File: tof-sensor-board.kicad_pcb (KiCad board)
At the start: 2 copper layers, 20 x 12 mm, 27 parts, among them U1 STM32F302K8U6, U2 LTC2875, U4 VL53L0X, X1 16MHz

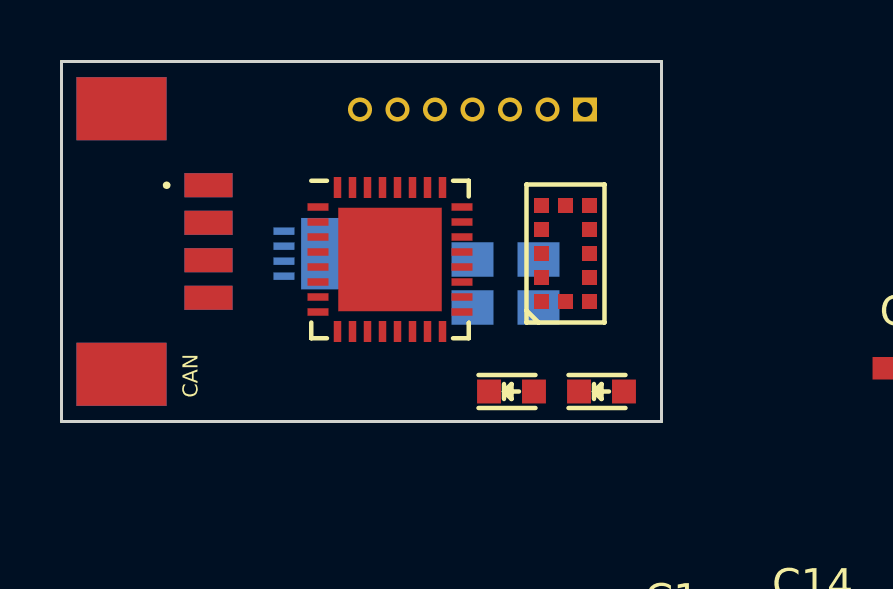
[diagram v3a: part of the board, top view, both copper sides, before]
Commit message: LDO footprint, fix unconnected GND pin
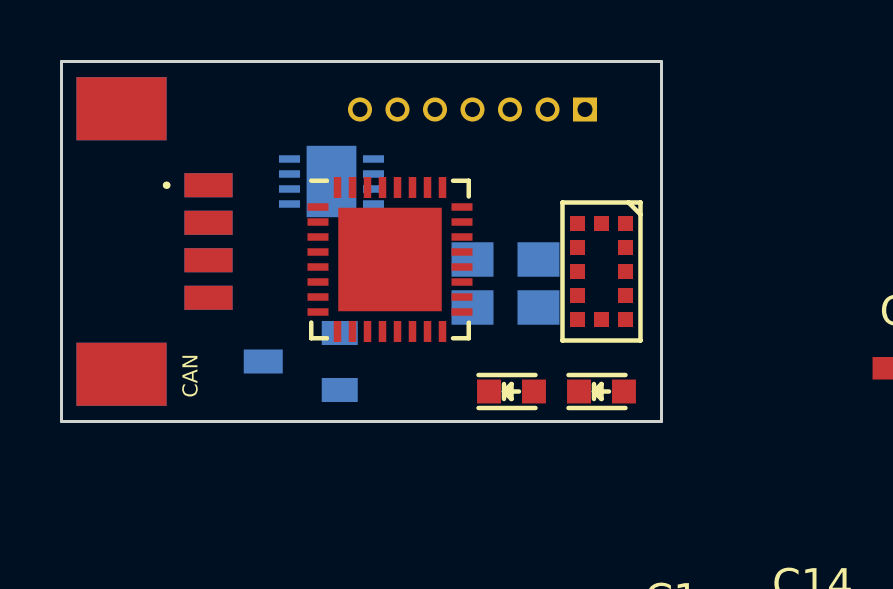
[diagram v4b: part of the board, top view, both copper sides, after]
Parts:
- added U3: MCP1703, _std:SOT-23, B.Cu at (39.0, 33.0)
- moved U2 2.41 mm to (40.0, 27.0)
- moved U4 1.34 mm to (49.0, 30.0), turned to 90 degrees
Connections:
- U4 pad 6: (no net) -> GND
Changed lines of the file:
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@@
 (kicad_pcb (version 4) (host pcbnew 4.0.1-stable)
   (general
-    (links 82)
-    (no_connects 82)
+    (links 86)
+    (no_connects 86)
     (area 30.949999 22.949999 51.050001 35.050001)
     (thickness 1.6)
@@
     (tracks 0)
     (zones 0)
-    (modules 27)
+    (modules 28)
     (nets 26)
   )
@@
   )
   (module Housings_DFN_QFN:DFN-8-1EP_3x3mm_Pitch0.5mm (layer B.Cu)
-    (at 39.815 29.405 180)
+    (at 40 27 180)
     (descr "DD Package; 8-Lead Plastic DFN (3mm x 3mm) (see Linear Technology DFN_8_05-08-1698.pdf)")
     (tags "DFN 0.5")
@@
   )
   (module _sensors:VL53L0X (layer F.Cu)
-    (at 47.8 29.4 270)
+    (at 49 30 90)
     (descr VL53L0X)
     (tags "TOF distance sensor")
-    (fp_text reference U4 (at 0 0 270) (layer F.SilkS) hide
+    (fp_text reference U4 (at 0 0 90) (layer F.SilkS) hide
       (effects (font (size 0.5 0.5) (thickness 0.125)))
     )
-    (fp_text value VL53L0X (at 0 0 270) (layer F.Fab) hide
+    (fp_text value VL53L0X (at 0 0 90) (layer F.Fab) hide
       (effects (font (size 0.5 0.5) (thickness 0.125)))
     )
@@
     (fp_line (start -2.3 -1.3) (end -2.3 1.3) (layer F.SilkS) (width 0.15))
     (fp_line (start 2.3 -1.3) (end -2.3 -1.3) (layer F.SilkS) (width 0.15))
-    (pad 1 smd rect (at 1.6 0.8 270) (size 0.5 0.5) (layers F.Cu F.Paste F.Mask)
-      (net 1 VCC))
-    (pad 2 smd rect (at 0.8 0.8 270) (size 0.5 0.5) (layers F.Cu F.Paste F.Mask)
-      (net 2 GND))
-    (pad 3 smd rect (at 0 0.8 270) (size 0.5 0.5) (layers F.Cu F.Paste F.Mask)
-      (net 2 GND))
-    (pad 5 smd rect (at -1.6 0.8 270) (size 0.5 0.5) (layers F.Cu F.Paste F.Mask)
+    (pad 1 smd rect (at 1.6 0.8 90) (size 0.5 0.5) (layers F.Cu F.Paste F.Mask)
+      (net 1 VCC))
+    (pad 2 smd rect (at 0.8 0.8 90) (size 0.5 0.5) (layers F.Cu F.Paste F.Mask)
+      (net 2 GND))
+    (pad 3 smd rect (at 0 0.8 90) (size 0.5 0.5) (layers F.Cu F.Paste F.Mask)
+      (net 2 GND))
+    (pad 5 smd rect (at -1.6 0.8 90) (size 0.5 0.5) (layers F.Cu F.Paste F.Mask)
       (net 22 /XSHUT))
-    (pad 4 smd rect (at -0.8 0.8 270) (size 0.5 0.5) (layers F.Cu F.Paste F.Mask)
-      (net 2 GND))
-    (pad 6 smd rect (at -1.6 0 270) (size 0.5 0.5) (layers F.Cu F.Paste F.Mask))
-    (pad 11 smd rect (at 1.6 -0.8 270) (size 0.5 0.5) (layers F.Cu F.Paste F.Mask)
-      (net 1 VCC))
-    (pad 10 smd rect (at 0.8 -0.8 270) (size 0.5 0.5) (layers F.Cu F.Paste F.Mask)
+    (pad 4 smd rect (at -0.8 0.8 90) (size 0.5 0.5) (layers F.Cu F.Paste F.Mask)
+      (net 2 GND))
+    (pad 6 smd rect (at -1.6 0 90) (size 0.5 0.5) (layers F.Cu F.Paste F.Mask)
+      (net 2 GND))
+    (pad 11 smd rect (at 1.6 -0.8 90) (size 0.5 0.5) (layers F.Cu F.Paste F.Mask)
+      (net 1 VCC))
+    (pad 10 smd rect (at 0.8 -0.8 90) (size 0.5 0.5) (layers F.Cu F.Paste F.Mask)
       (net 16 /I2C_SCL))
-    (pad 9 smd rect (at 0 -0.8 270) (size 0.5 0.5) (layers F.Cu F.Paste F.Mask)
+    (pad 9 smd rect (at 0 -0.8 90) (size 0.5 0.5) (layers F.Cu F.Paste F.Mask)
       (net 17 /I2C_SDA))
-    (pad 8 smd rect (at -0.8 -0.8 270) (size 0.5 0.5) (layers F.Cu F.Paste F.Mask))
-    (pad 7 smd rect (at -1.6 -0.8 270) (size 0.5 0.5) (layers F.Cu F.Paste F.Mask)
+    (pad 8 smd rect (at -0.8 -0.8 90) (size 0.5 0.5) (layers F.Cu F.Paste F.Mask))
+    (pad 7 smd rect (at -1.6 -0.8 90) (size 0.5 0.5) (layers F.Cu F.Paste F.Mask)
       (net 15 /GPIO1))
-    (pad 12 smd rect (at 1.6 0 270) (size 0.5 0.5) (layers F.Cu F.Paste F.Mask)
+    (pad 12 smd rect (at 1.6 0 90) (size 0.5 0.5) (layers F.Cu F.Paste F.Mask)
       (net 2 GND))
   )
@@
     )
   )
+  (module _std:SOT-23 (layer B.Cu)
+    (at 39 33 270)
+    (descr "SOT-23, Standard")
+    (tags SOT-23)
+    (attr smd)
+    (fp_text reference U3 (at 0 3 270) (layer B.SilkS) hide
+      (effects (font (size 1 1) (thickness 0.15)) (justify mirror))
+    )
+    (fp_text value MCP1703 (at 0 -3 270) (layer B.Fab) hide
+      (effects (font (size 1 1) (thickness 0.15)) (justify mirror))
+    )
+    (fp_line (start 1.29916 0.65024) (end 1.2509 0.65024) (layer B.SilkS) (width 0.15))
+    (fp_line (start -1.49982 -0.0508) (end -1.49982 0.65024) (layer B.SilkS) (width 0.15))
+    (fp_line (start -1.49982 0.65024) (end -1.2509 0.65024) (layer B.SilkS) (width 0.15))
+    (fp_line (start 1.29916 0.65024) (end 1.49982 0.65024) (layer B.SilkS) (width 0.15))
+    (fp_line (start 1.49982 0.65024) (end 1.49982 -0.0508) (layer B.SilkS) (width 0.15))
+    (pad 1 smd rect (at -0.95 -1.275 270) (size 0.8 1.2) (layers B.Cu B.Paste B.Mask)
+      (net 2 GND))
+    (pad 2 smd rect (at 0.95 -1.275 270) (size 0.8 1.2) (layers B.Cu B.Paste B.Mask)
+      (net 1 VCC))
+    (pad 3 smd rect (at 0 1.275 270) (size 0.8 1.3) (layers B.Cu B.Paste B.Mask)
+      (net 4 +5V))
+    (model Housings_SOT-23_SOT-143_TSOT-6.3dshapes/SOT-23.wrl
+      (at (xyz 0 0 0))
+      (scale (xyz 1 1 1))
+      (rotate (xyz 0 0 0))
+    )
+  )

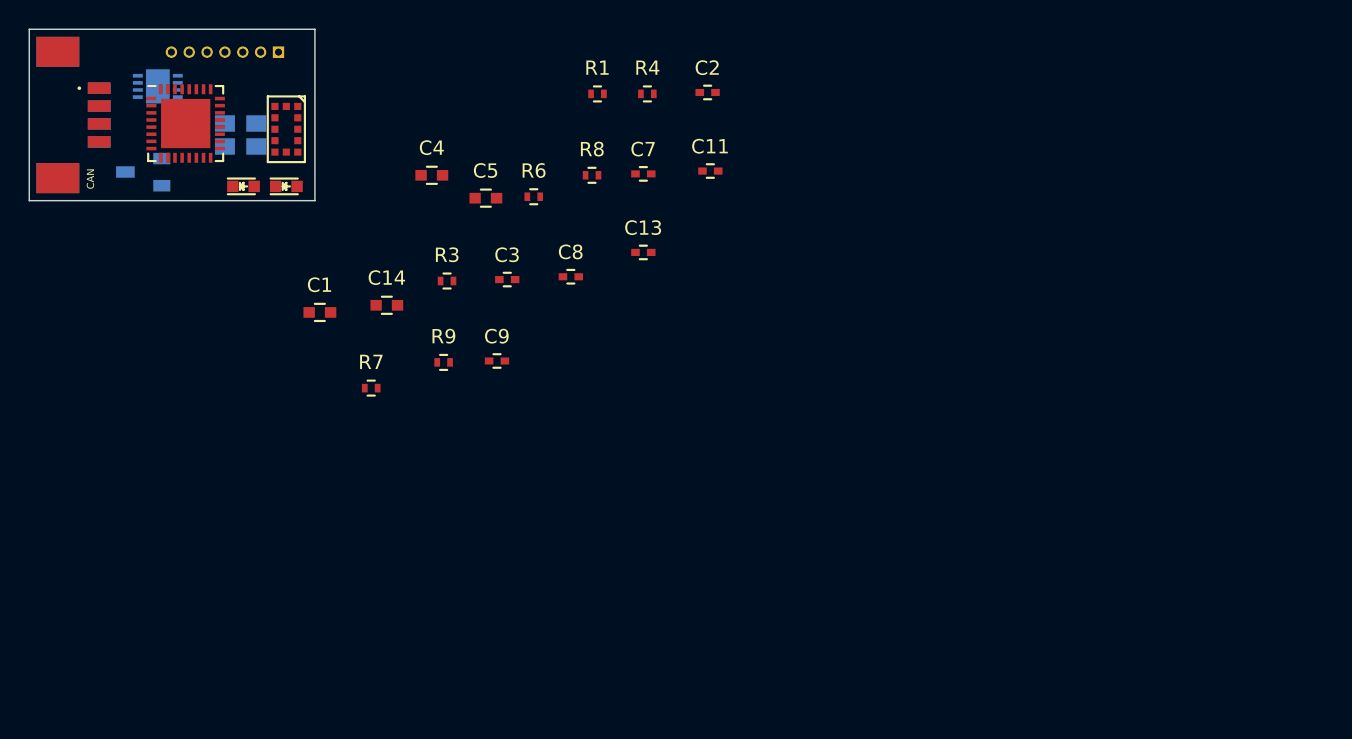
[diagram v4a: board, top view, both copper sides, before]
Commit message: Place mounting holes
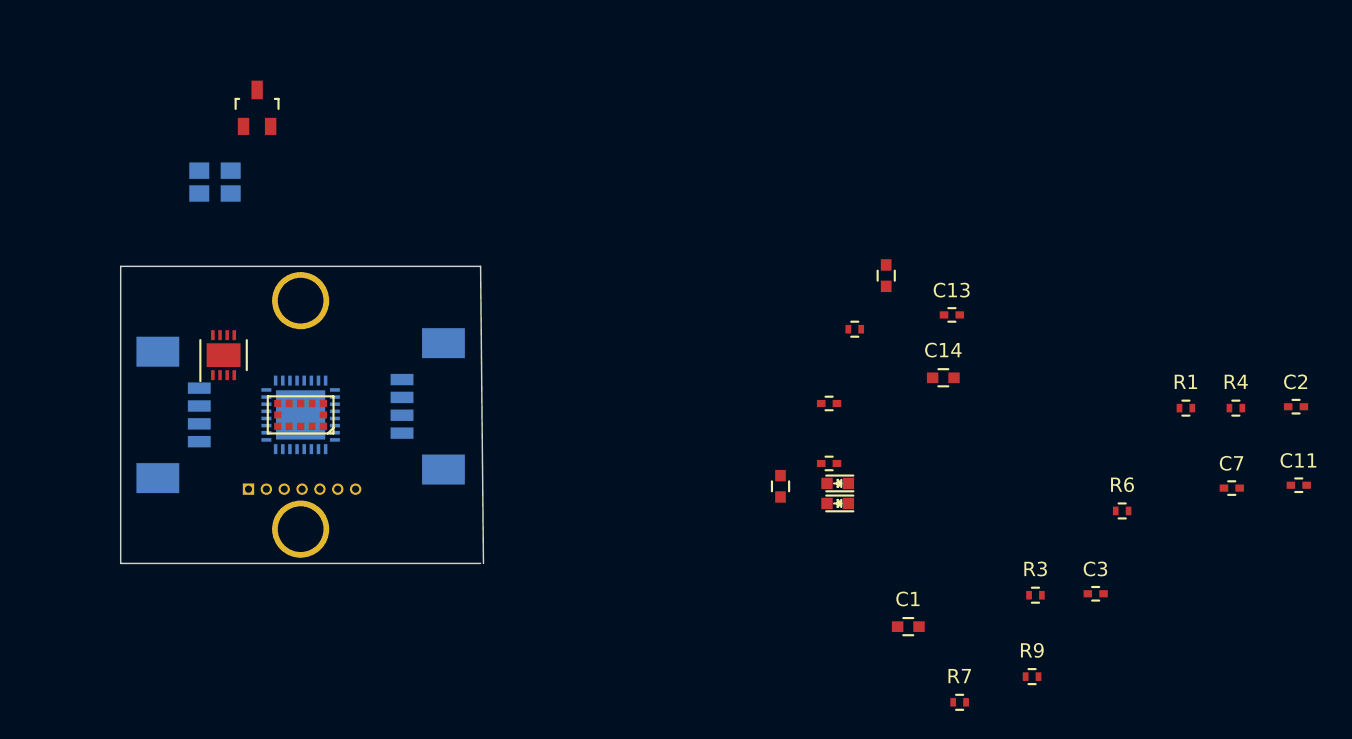
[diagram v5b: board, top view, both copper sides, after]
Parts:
- added CVRA-HOLE: VAL**, cvra:CVRA-HOLE, F.Cu at (50.0, 42.0)
- added CVRA-HOLE: VAL**, cvra:CVRA-HOLE, F.Cu at (50.0, 58.0)
- CONN3, U1: moved to B.Cu
- U2, U3: moved to F.Cu
- moved D2 47.2 mm to (87.6, 56.2), turned to 180 degrees
- moved R3 46.7 mm to (101.5, 62.6)
- moved R7 46.7 mm to (96.1, 70.1)
- moved R9 46.7 mm to (101.2, 68.3)
- moved C1 46.7 mm to (92.5, 64.8)
- moved C2 46.7 mm to (119.7, 49.4)
- moved C3 46.7 mm to (105.7, 62.5)
- moved C7 46.7 mm to (115.2, 55.1)
- moved R4 46.7 mm to (115.5, 49.5)
- moved R6 46.7 mm to (107.5, 56.7)
- moved C11 46.7 mm to (119.9, 54.9)
- moved R1 46.7 mm to (112.0, 49.5)
- moved D3 43.8 mm to (87.6, 54.8), turned to 180 degrees
- moved C14 39.3 mm to (95.0, 47.4)
- moved CONN3 33.8 mm to (60.0, 49.4)
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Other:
- board size 20 x 12 mm -> 25.4 x 20.8 mm
- net class Default: clearance 0.2 -> 0.16; trace_width 0.25 -> 0.16; via_drill 0.4 -> 0.3
- rule trace_clearance: 0.2 -> 0.16
- rule trace_min: 0.15 -> 0.1524
- rule via_min_size: 0.4 -> 0.6

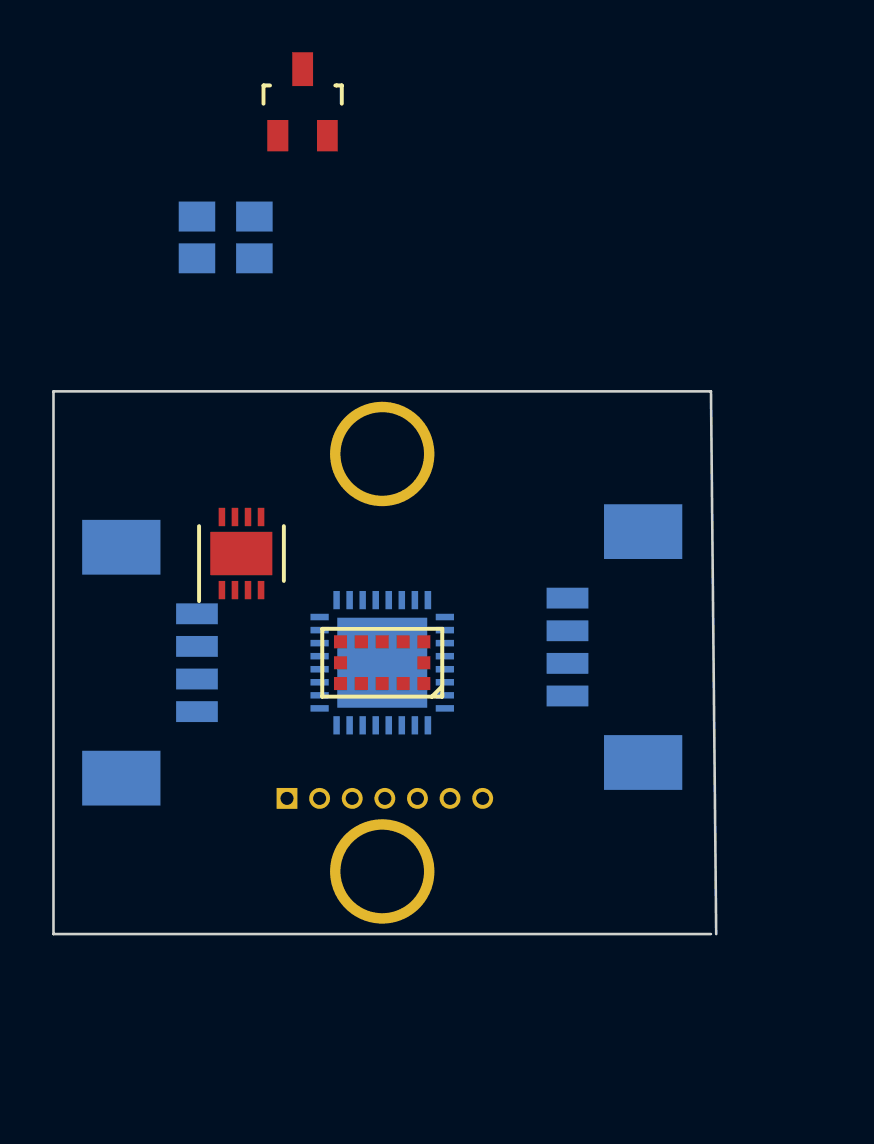
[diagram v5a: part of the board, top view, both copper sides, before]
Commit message: elongated shape with connectors on same edge
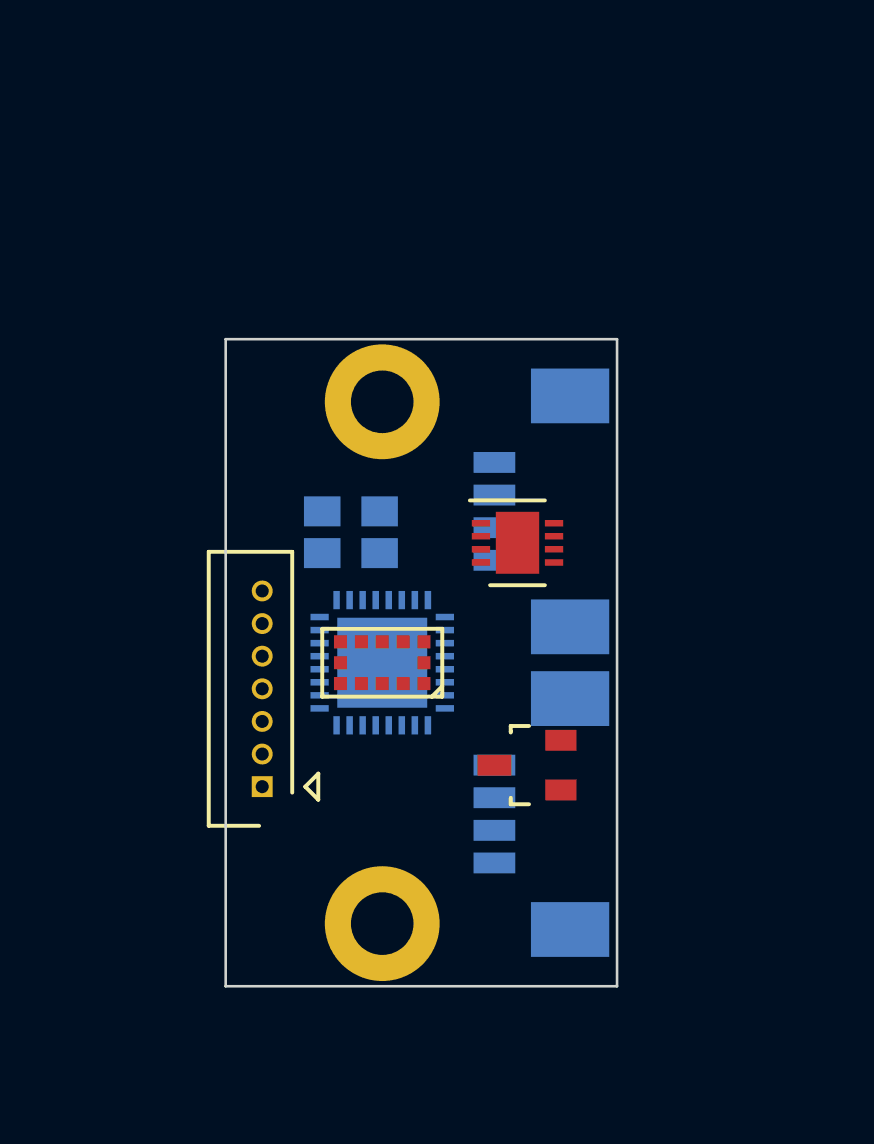
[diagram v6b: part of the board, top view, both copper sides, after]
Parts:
- removed CVRA-HOLE (x2): VAL**, cvra:CVRA-HOLE
- added _M2: VAL**, _mech:_M2, F.Cu at (50.4, 40.0)
- added _M2: VAL**, _mech:_M2, F.Cu at (50.0, 60.0)
- CONN1: moved to F.Cu
- moved U3 26.8 mm to (55.6, 53.9), turned to 90 degrees
- moved CONN2 18.2 mm to (57.2, 44.2), turned to 270 degrees
- moved X1 12.3 mm to (48.8, 45.0)
- moved U2 10.6 mm to (55.2, 45.4), turned to 0 degrees
- moved CONN3 6.99 mm to (57.2, 55.8)
- moved CONN1 1.05 mm to (45.4, 54.8), turned to 90 degrees
- turned U1 to 270 degrees
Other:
- board size 25.4 x 20.8 mm -> 15 x 24.8 mm

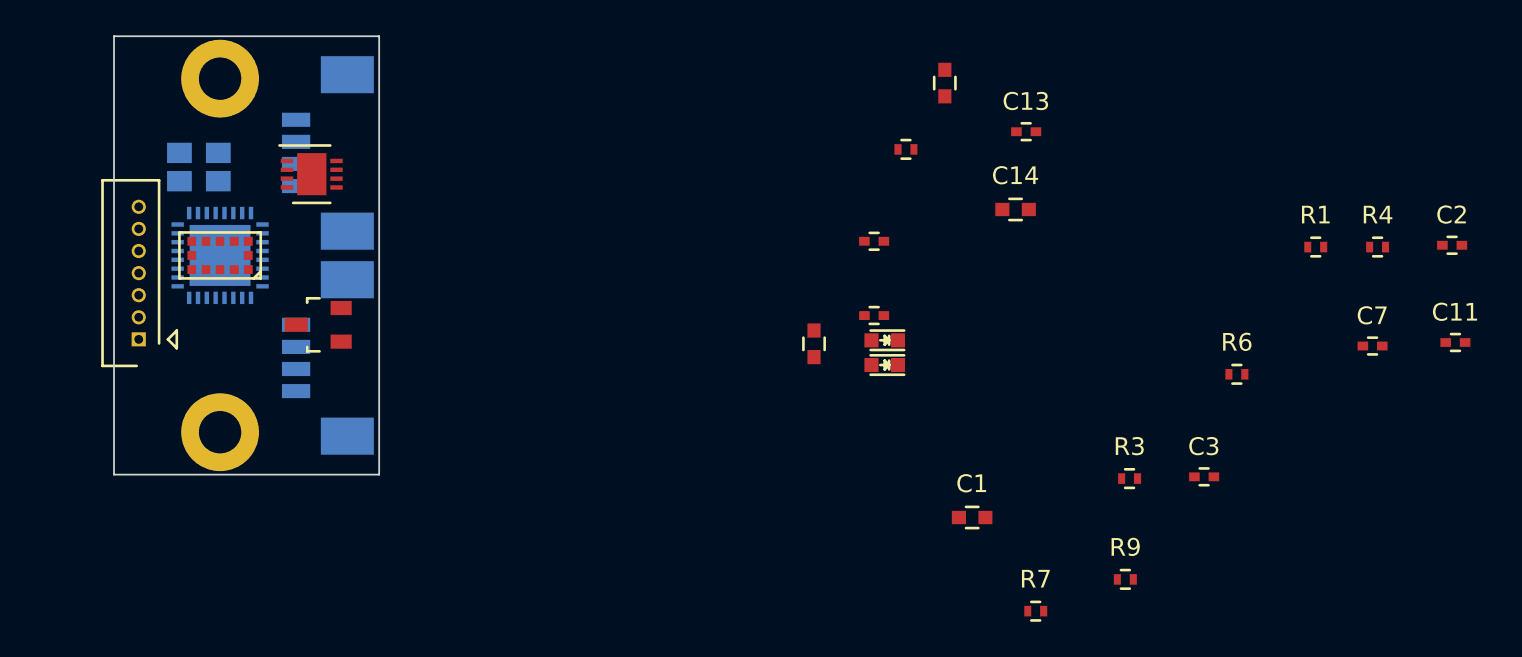
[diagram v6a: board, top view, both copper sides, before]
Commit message: mounting holes on same edge
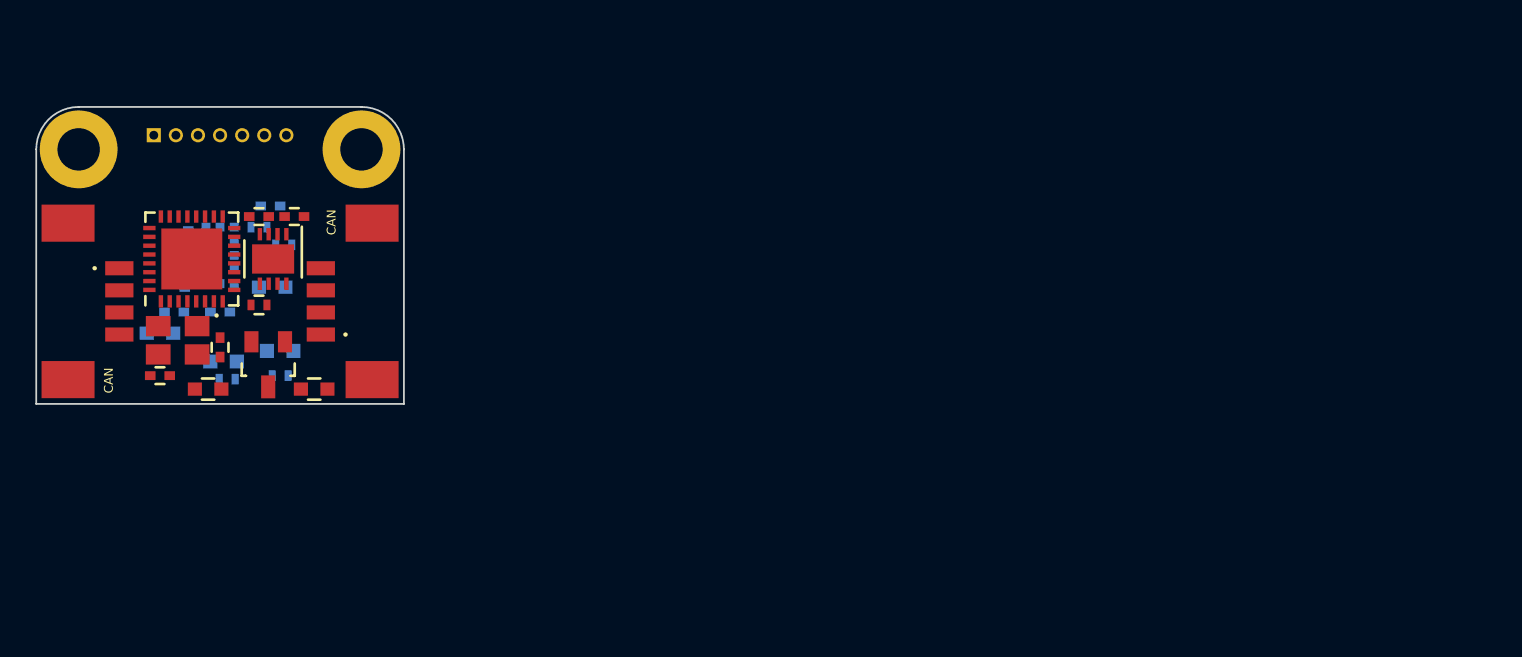
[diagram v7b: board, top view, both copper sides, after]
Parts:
- C1, C13, C14, C3, C7, CONN1, D2, D3, R1, R3, R4, R6, R7, R9, U4: moved to B.Cu
- CONN2, CONN3, U1, X1: moved to F.Cu
- moved C2 67.5 mm to (52.2, 47.8)
- moved R4 67.3 mm to (48.2, 49.0), turned to 270 degrees
- moved C11 66.1 mm to (54.2, 47.8)
- moved C7 62.8 mm to (52.9, 47.2)
- moved C3 59.0 mm to (47.4, 53.2), turned to 180 degrees
- moved R1 58.4 mm to (53.6, 49.4), turned to 180 degrees
- moved R6 57.1 mm to (50.4, 57.0)
- moved R3 54.6 mm to (48.0, 51.4), turned to 90 degrees
- moved R9 52.9 mm to (52.2, 48.4), turned to 180 degrees
- moved C1 47.1 mm to (46.6, 54.4)
- moved C13 46.7 mm to (50.0, 53.2)
- moved R7 44.8 mm to (53.4, 56.8), turned to 180 degrees
- moved C14 42.3 mm to (53.0, 51.8)
- moved C9 40.5 mm to (46.6, 56.8), turned to 0 degrees
- moved C4 39.7 mm to (55.3, 57.6), turned to 0 degrees
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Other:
- board size 15 x 24.8 mm -> 20.8 x 16.8 mm
